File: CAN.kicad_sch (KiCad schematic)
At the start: 14 parts, among them J300 MCP_EXTERNAL, J301 CAN_INPUT, U300 MCP2515-xSO, U301 TJA1050, Y300 8MHz

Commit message: added BOM, Gerber and modified a few footprints
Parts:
- added TP300, TP301: TestPoint, TestPoint:TestPoint_Pad_D2.0mm, symbol Connector:TestPoint
- C300: footprint Capacitor_SMD:C_0805_2012Metric -> Capacitor_SMD:C_0603_1608Metric; LCSC C7171 -> C19702
- C301, C304: value 0.1u -> 100n; LCSC C24497 -> C1525
- C302, C303: LCSC (none) -> C32949
- C305: LCSC (none) -> C1744
- R300: LCSC C17902 -> C25804
- U301: LCSC (none) -> C6952
- Y300: LCSC (none) -> C400090
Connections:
- net CANH: now also TP300.1
- net CANL: now also TP301.1
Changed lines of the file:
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@@
   (junction (at 198.628 68.834) (diameter 0) (color 0 0 0 0)
   )
+  (junction (at 209.55 92.075) (diameter 0) (color 0 0 0 0)
+  )
   (junction (at 167.259 91.059) (diameter 0) (color 0 0 0 0)
   )
@@
   )
   (junction (at 198.628 77.724) (diameter 0) (color 0 0 0 0)
+  )
+  (junction (at 209.423 68.834) (diameter 0) (color 0 0 0 0)
   )
   (junction (at 198.628 86.614) (diameter 0) (color 0 0 0 0)
@@
     (stroke (width 0) (type default) (color 0 0 0 0))
   )
+  (wire (pts (xy 209.423 68.834) (xy 198.628 68.834))
+    (stroke (width 0) (type default) (color 0 0 0 0))
+  )
   (wire (pts (xy 66.167 105.791) (xy 66.167 108.331))
     (stroke (width 0) (type default) (color 0 0 0 0))
@@
     (stroke (width 0) (type default) (color 0 0 0 0))
   )
+  (wire (pts (xy 209.55 92.075) (xy 209.55 100.33))
+    (stroke (width 0) (type default) (color 0 0 0 0))
+  )
   (wire (pts (xy 198.628 77.724) (xy 198.628 78.994))
     (stroke (width 0) (type default) (color 0 0 0 0))
@@
     (stroke (width 0) (type default) (color 0 0 0 0))
   )
+  (wire (pts (xy 209.55 92.075) (xy 198.628 92.075))
+    (stroke (width 0) (type default) (color 0 0 0 0))
+  )
   (wire (pts (xy 116.205 98.171) (xy 119.38 98.171))
     (stroke (width 0) (type default) (color 0 0 0 0))
@@
     (stroke (width 0) (type default) (color 0 0 0 0))
   )
-  (wire (pts (xy 211.836 68.834) (xy 198.628 68.834))
+  (wire (pts (xy 211.836 68.834) (xy 209.423 68.834))
     (stroke (width 0) (type default) (color 0 0 0 0))
   )
@@
     (stroke (width 0) (type default) (color 0 0 0 0))
   )
+  (wire (pts (xy 209.423 59.563) (xy 209.423 68.834))
+    (stroke (width 0) (type default) (color 0 0 0 0))
+  )
   (polyline (pts (xy 50.419 140.589) (xy 86.487 140.589))
     (stroke (width 0) (type default) (color 0 0 0 0))
@@
     (stroke (width 0) (type default) (color 0 0 0 0))
   )
-  (wire (pts (xy 219.075 92.075) (xy 198.628 92.075))
+  (wire (pts (xy 219.075 92.075) (xy 209.55 92.075))
     (stroke (width 0) (type default) (color 0 0 0 0))
   )
@@
       (effects (font (size 1.27 1.27)) hide)
     )
+    (property "LCSC" "C1744" (id 4) (at 206.248 81.534 0)
+      (effects (font (size 1.27 1.27)) hide)
+    )
     (pin "1")
     (pin "2")
@@
       (effects (font (size 1.27 1.27)) hide)
     )
-    (property "LCSC" " C17902" (id 4) (at 121.92 98.171 90)
+    (property "LCSC" "C25804" (id 4) (at 121.92 98.171 90)
       (effects (font (size 1.27 1.27)) hide)
     )
@@
       (effects (font (size 1.27 1.27)) (justify left))
     )
-    (property "Value" "0.1u" (id 1) (at 158.877 62.103 90)
+    (property "Value" "100n" (id 1) (at 158.877 62.103 90)
       (effects (font (size 1.27 1.27)) (justify left))
     )
@@
       (effects (font (size 1.27 1.27)) hide)
     )
-    (property "LCSC" "C24497" (id 4) (at 161.417 65.913 0)
+    (property "LCSC" "C1525" (id 4) (at 161.417 65.913 90)
       (effects (font (size 1.27 1.27)) hide)
     )
@@
       (effects (font (size 1.27 1.27)) hide)
     )
-    (pin "1")
-    (pin "2")
+    (property "LCSC" "C32949" (id 4) (at 78.867 108.331 0)
+      (effects (font (size 1.27 1.27)) hide)
+    )
+    (pin "1")
+    (pin "2")
+  )
+  (symbol (lib_id "Connector:TestPoint") (at 209.55 100.33 180) (unit 1)
+    (in_bom yes) (on_board yes)
+    (property "Reference" "TP301" (id 0) (at 212.344 108.458 0)
+      (effects (font (size 1.27 1.27)) (justify left))
+    )
+    (property "Value" "TestPoint" (id 1) (at 213.741 105.791 0)
+      (effects (font (size 1.27 1.27)) (justify left))
+    )
+    (property "Footprint" "TestPoint:TestPoint_Pad_D2.0mm" (id 2) (at 204.47 100.33 0)
+      (effects (font (size 1.27 1.27)) hide)
+    )
+    (property "Datasheet" "~" (id 3) (at 204.47 100.33 0)
+      (effects (font (size 1.27 1.27)) hide)
+    )
+    (pin "1")
   )
   (symbol (lib_id "power:GND") (at 157.099 66.675 0) (unit 1)
@@
       (effects (font (size 1.27 1.27)) (justify left))
     )
-    (property "Value" "0.1u" (id 1) (at 94.869 57.023 0)
+    (property "Value" "100n" (id 1) (at 94.869 57.023 0)
       (effects (font (size 1.27 1.27)) (justify left))
     )
@@
       (effects (font (size 1.27 1.27)) hide)
     )
-    (property "LCSC" "C24497" (id 4) (at 93.345 54.991 0)
+    (property "LCSC" "C1525" (id 4) (at 93.345 54.991 0)
       (effects (font (size 1.27 1.27)) hide)
     )
@@
     (pin "1")
   )
+  (symbol (lib_id "Connector:TestPoint") (at 209.423 59.563 0) (unit 1)
+    (in_bom yes) (on_board yes)
+    (property "Reference" "TP300" (id 0) (at 206.629 51.435 0)
+      (effects (font (size 1.27 1.27)) (justify left))
+    )
+    (property "Value" "TestPoint" (id 1) (at 205.232 54.102 0)
+      (effects (font (size 1.27 1.27)) (justify left))
+    )
+    (property "Footprint" "TestPoint:TestPoint_Pad_D2.0mm" (id 2) (at 214.503 59.563 0)
+      (effects (font (size 1.27 1.27)) hide)
+    )
+    (property "Datasheet" "~" (id 3) (at 214.503 59.563 0)
+      (effects (font (size 1.27 1.27)) hide)
+    )
+    (pin "1")
+  )
   (symbol (lib_id "Device:Crystal_GND24") (at 66.167 100.711 0) (unit 1)
     (in_bom yes) (on_board yes)
@@
       (effects (font (size 1.27 1.27)) hide)
     )
-    (property "LCSC Part #" "" (id 4) (at 66.167 100.711 0)
+    (property "LCSC" "C400090" (id 4) (at 66.167 100.711 0)
       (effects (font (size 1.27 1.27)) hide)
     )
@@
       (effects (font (size 1.27 1.27)) (justify left))
     )
-    (property "Footprint" "Capacitor_SMD:C_0805_2012Metric" (id 2) (at 88.265 54.991 0)
+    (property "Footprint" "Capacitor_SMD:C_0603_1608Metric" (id 2) (at 88.265 54.991 0)
       (effects (font (size 1.27 1.27)) hide)
     )
@@
       (effects (font (size 1.27 1.27)) hide)
     )
-    (property "LCSC" "C7171" (id 4) (at 88.265 54.991 0)
+    (property "LCSC" "C19702" (id 4) (at 88.265 54.991 0)
       (effects (font (size 1.27 1.27)) hide)
     )
@@
     )
     (property "Datasheet" "" (id 3) (at 167.259 79.883 0)
+      (effects (font (size 1.27 1.27)) hide)
+    )
+    (property "LCSC" "C6952" (id 4) (at 167.259 79.883 0)
       (effects (font (size 1.27 1.27)) hide)
     )
@@
       (effects (font (size 1.27 1.27)) hide)
     )
+    (property "LCSC" "C32949" (id 4) (at 53.467 108.331 0)
+      (effects (font (size 1.27 1.27)) hide)
+    )

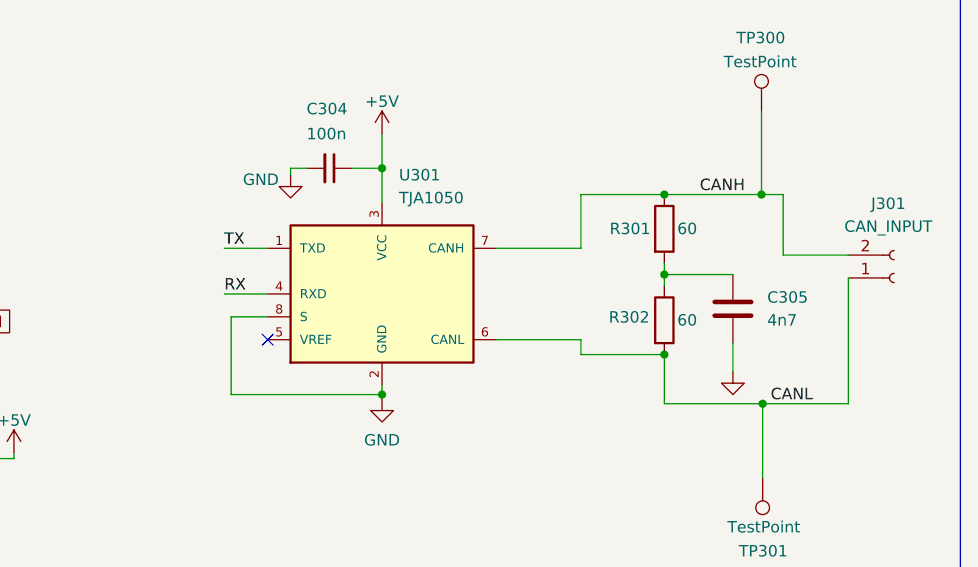
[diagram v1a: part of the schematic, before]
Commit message: change names and move WIZ850 position
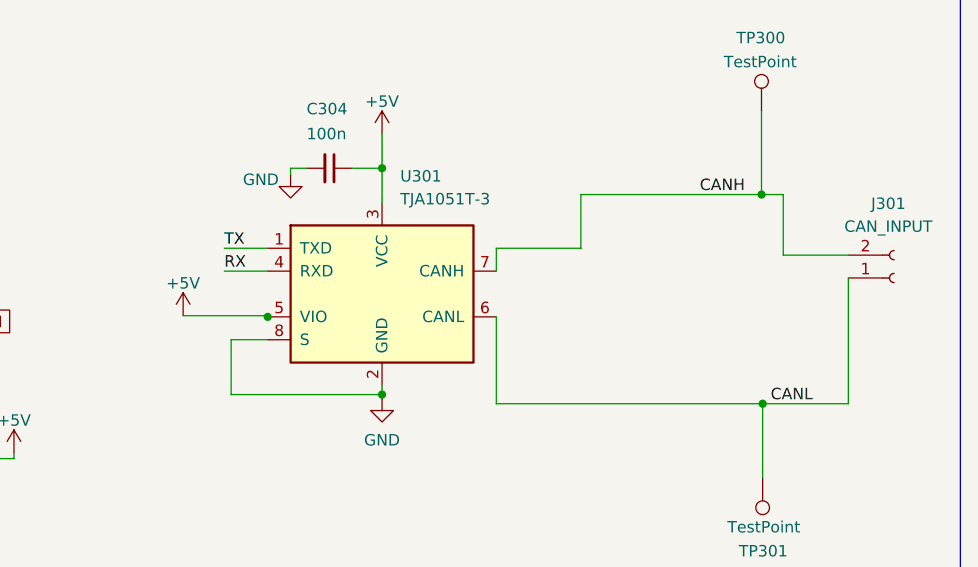
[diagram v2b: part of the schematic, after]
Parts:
- removed C305: 4n7, Capacitor_SMD:C_0805_2012Metric, symbol Device:C
- removed R301, R302: 60, Resistor_SMD:R_0402_1005Metric, symbol Device:R
- removed U301: TJA1050, TJA1050T:SOT96-1, symbol TJA1050T:TJA1050
- added U301: TJA1051T-3, Package_SO:SOIC-8_3.9x4.9mm_P1.27mm, symbol Interface_CAN_LIN:TJA1051T-3
- U300: LCSC C153782 -> C12368
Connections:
- net +5V: now also U301.3 (VCC), U301.5 (VIO)
- net CANH: now also U301.7 (CANH)
- net CANL: now also U301.6 (CANL)
- net GND: now also U301.2 (GND), U301.8 (S)
- net RX: now also U301.4 (RXD)
- net TX: now also U301.1 (TXD)
- no-connect marks 7 -> 6
